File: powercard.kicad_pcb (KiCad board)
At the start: 4 copper layers, 90 x 54.3 mm, 105 parts, among them J1 EDGE, J2 PDI, J3 DBG, Q1 CSD18503Q5A, Q2 CSD18503Q5A, Q3 CSD18503Q5A, Q4 CSD18503Q5A, Q5 BSS84, Q6 2N7002, Q7 2N7002, U1 RT7258GQW, U2 RT7258GQW, U3 RT7258GQW, U4 RT7258GQW, U5 74HCT1G02, U6 RT7258GQW, U7 ATXMEGA32E5-MU, U8 MCP1754ST-3302E/CB

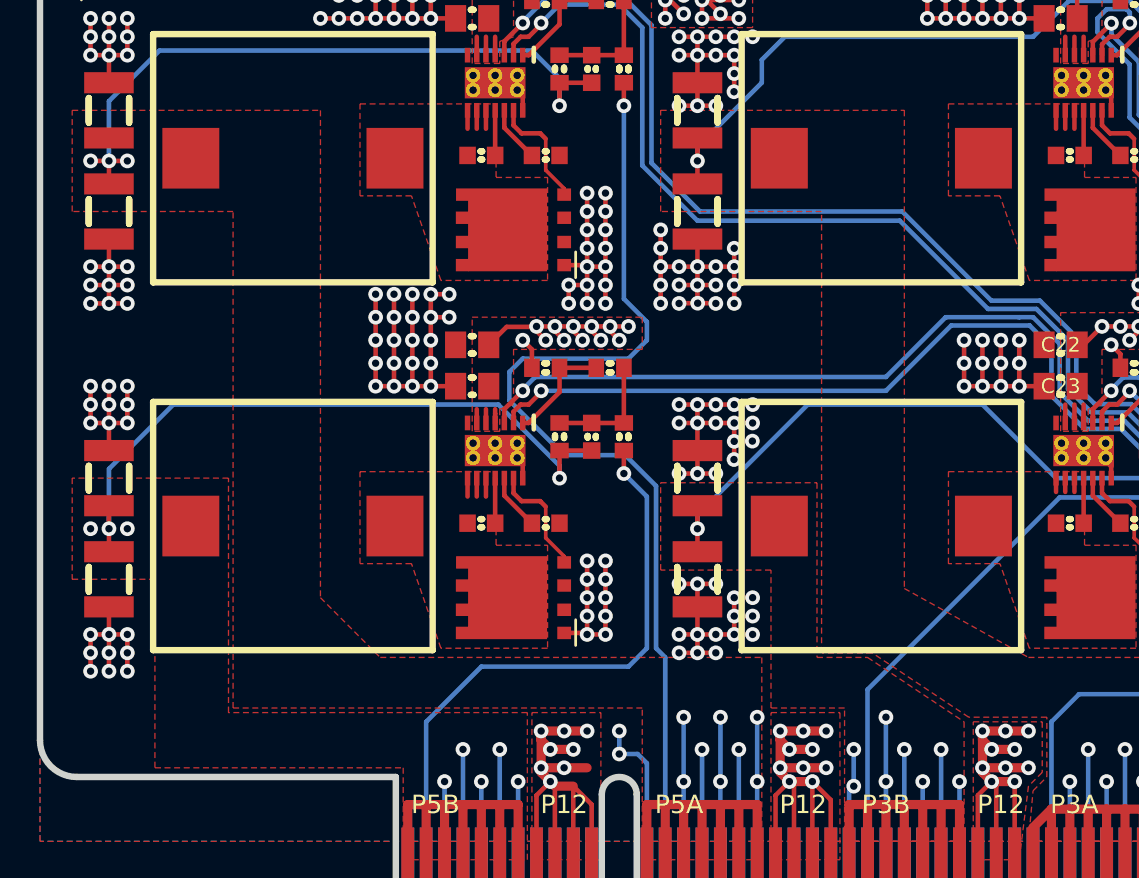
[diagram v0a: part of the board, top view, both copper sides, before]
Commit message: Layout tweaks
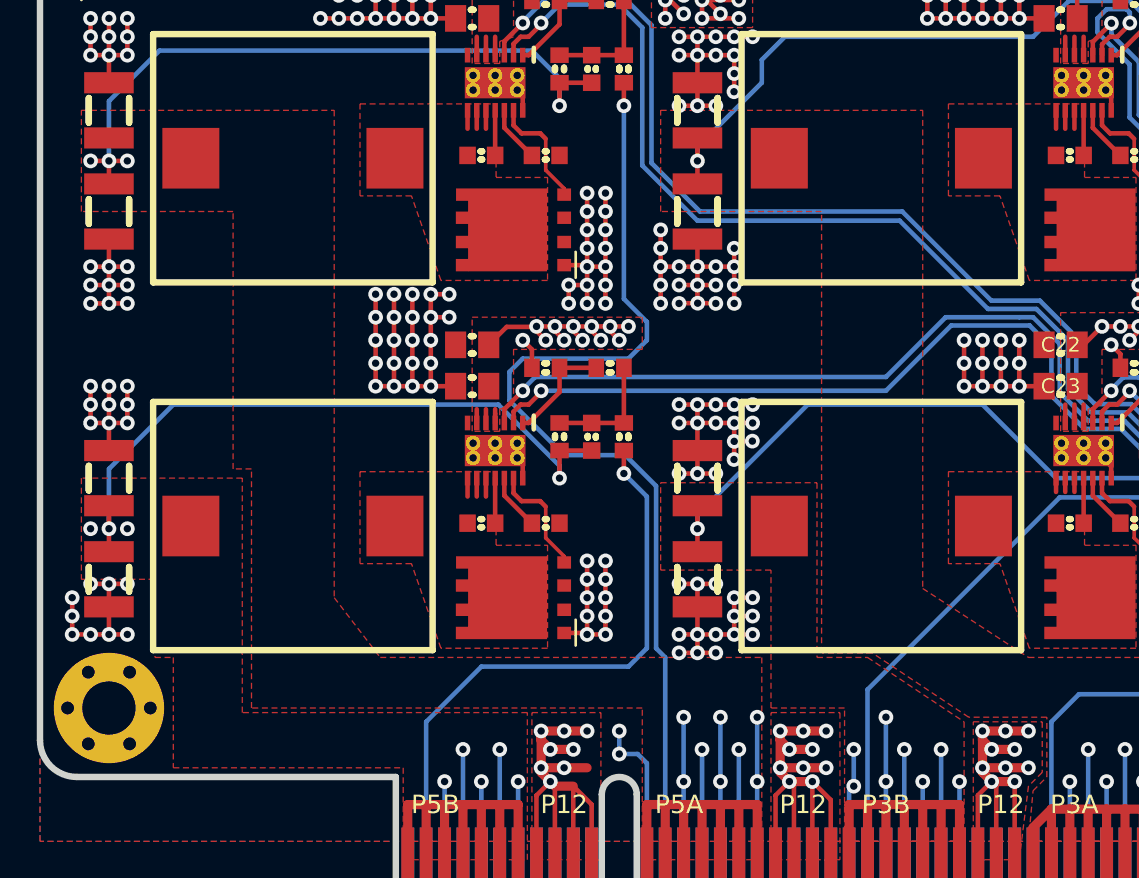
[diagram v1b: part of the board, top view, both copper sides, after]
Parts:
- added MP1: SCREW, mech:SCREW-3-SUPPORTED, F.Cu at (51.8, 89.2)

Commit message: More PCB tweaks
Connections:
- J1 pad A45: Net-(J1-PadA45) -> GND
- J1 pad A46: /INT# -> GND
- J1 pad A47: /SCL -> /INT#
- J1 pad A48: /SDA -> /SCL
- J1 pad A49: GND -> /SDA
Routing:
- net GND: track 493.8 -> 496.5 mm, vias 305 -> 317
- net /INT#: track 16.3 -> 14.6 mm
- net /SCL: track 16.2 -> 15.1 mm
- net /SDA: track 15.7 -> 15.1 mm
- net /N12V_1A: vias 13 -> 12
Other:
- board text added: "+12"
- board text added: "+3A"
- board text added: "+3B"
- board text added: "+5A"
- board text added: "+5B"
- board text added: "12"
- board text removed: "G"
- board text removed: "INT"
- board text removed: "N12"
- board text removed: "N12s"
- board text removed: "P12"
- board text removed: "P3A"
- board text removed: "P3As"
- board text removed: "P3B"
- board text removed: "P3Bs"
- board text removed: "P5A"
- board text removed: "P5As"
- board text removed: "P5B"
- board text removed: "P5Bs"
- board text removed: "SCL"
- board text removed: "SDA"

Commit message: Even more PCB tweaks
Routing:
- net GND: track 496.5 -> 497.5 mm
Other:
- board text added: "A 3V3 B"
- board text added: "A 5V B"
- board text added: "C4-0 POWER SUPPLY REV 1.0 JULY 2016"
- board text added: "N12"
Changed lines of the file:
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@@
     (area 47.824999 46.824999 138.175001 101.525001)
     (thickness 1.6)
-    (drawings 112)
-    (tracks 1902)
+    (drawings 150)
+    (tracks 1910)
     (zones 0)
     (modules 106)
@@
     (35 F.Paste user)
     (36 B.SilkS user)
-    (37 F.SilkS user)
+    (37 F.SilkS user hide)
     (38 B.Mask user)
     (39 F.Mask user)
@@
     (45 Margin user)
     (46 B.CrtYd user)
-    (47 F.CrtYd user hide)
+    (47 F.CrtYd user)
     (48 B.Fab user)
     (49 F.Fab user hide)
@@
     )
   )
+  (gr_line (start 107 90.75) (end 107.75 91) (layer F.Mask) (width 0.5))
+  (gr_line (start 107 92.25) (end 107.75 92) (layer F.Mask) (width 0.5))
+  (gr_line (start 107.75 90.5) (end 107.75 92.25) (layer F.Mask) (width 0.5))
+  (gr_line (start 108 92.25) (end 107 92.5) (layer F.Mask) (width 0.5))
+  (gr_line (start 108 90.5) (end 108 92.25) (layer F.Mask) (width 0.5))
+  (gr_line (start 107 90.5) (end 107.75 90.5) (layer F.Mask) (width 1))
+  (gr_line (start 106 90.75) (end 107 90.5) (layer F.Mask) (width 1))
+  (gr_line (start 105 90.5) (end 106 90.75) (layer F.Mask) (width 1))
+  (gr_line (start 104 90.75) (end 105 90.5) (layer F.Mask) (width 1))
+  (gr_line (start 94 88.75) (end 95 89) (layer F.Mask) (width 1))
+  (gr_line (start 93 89) (end 94 88.75) (layer F.Mask) (width 1))
+  (gr_line (start 50.75 51.5) (end 50.75 52) (layer F.Mask) (width 0.2))
+  (gr_line (start 51 52) (end 50.75 51.5) (layer F.Mask) (width 0.2))
+  (gr_line (start 50.5 52) (end 51 52) (layer F.Mask) (width 0.2))
+  (gr_line (start 50.75 51.5) (end 50.5 52) (layer F.Mask) (width 0.2))
+  (gr_line (start 127.25 59.75) (end 127.25 60.25) (layer F.Mask) (width 0.2))
+  (gr_line (start 127.25 60.25) (end 127 60) (layer F.Mask) (width 0.2))
+  (gr_line (start 127 60) (end 127.25 59.75) (layer F.Mask) (width 0.2))
+  (gr_line (start 128.5 84) (end 129.25 84) (layer F.Mask) (width 0.2))
+  (gr_line (start 129.25 84.25) (end 128.5 84) (layer F.Mask) (width 0.2))
+  (gr_line (start 129.25 83.75) (end 129.25 84.25) (layer F.Mask) (width 0.2))
+  (gr_line (start 128.5 84) (end 129.25 83.75) (layer F.Mask) (width 0.2))
+  (gr_line (start 75.25 54.25) (end 75.25 54.75) (layer F.Mask) (width 0.2))
+  (gr_line (start 75 54.5) (end 75.25 54.25) (layer F.Mask) (width 0.2))
+  (gr_line (start 75.25 54.75) (end 75 54.5) (layer F.Mask) (width 0.2))
+  (gr_line (start 75.25 74.25) (end 75.25 74.75) (layer F.Mask) (width 0.2))
+  (gr_line (start 75 74.5) (end 75.25 74.25) (layer F.Mask) (width 0.2))
+  (gr_line (start 75.25 74.75) (end 75 74.5) (layer F.Mask) (width 0.2))
+  (gr_line (start 107.25 74.25) (end 107.25 74.75) (layer F.Mask) (width 0.2))
+  (gr_line (start 107 74.5) (end 107.25 74.25) (layer F.Mask) (width 0.2))
+  (gr_line (start 107.25 74.75) (end 107 74.5) (layer F.Mask) (width 0.2))
+  (gr_line (start 107 54.25) (end 107.25 54) (layer F.Mask) (width 0.2))
+  (gr_line (start 107.25 54.5) (end 107 54.25) (layer F.Mask) (width 0.2))
+  (gr_line (start 107.25 54) (end 107.25 54.5) (layer F.Mask) (width 0.2))
+  (gr_text N12 (at 124.5 49.75 90) (layer F.Mask)
+    (effects (font (size 1.1 1.1) (thickness 0.275)))
+  )
+  (gr_text "A\n3V3\nB" (at 88.5 69.5) (layer F.Mask)
+    (effects (font (size 1.1 1.1) (thickness 0.275)))
+  )
+  (gr_text "A\n5V\nB" (at 56 69.5) (layer F.Mask)
+    (effects (font (size 1.1 1.1) (thickness 0.275)))
+  )
+  (gr_text "C4-0 POWER SUPPLY\nREV 1.0 JULY 2016" (at 65.25 59.5) (layer B.Mask)
+    (effects (font (size 1.5 1.5) (thickness 0.3)) (justify mirror))
+  )
   (gr_line (start 113.25 93.5) (end 114.25 93.5) (layer F.Mask) (width 0.2))
   (gr_line (start 103.25 92.5) (end 103 94.75) (layer F.Mask) (width 0.75))
@@
   (segment (start 67.99826 97.75) (end 67.99826 94.50174) (width 0.5) (layer F.Cu) (net 1))
   (segment (start 76.25 75.25) (end 78 75.25) (width 0.25) (layer F.Cu) (net 1))
+  (segment (start 52.75 51.75) (end 53.75 51.75) (width 0.25) (layer F.Cu) (net 2))
+  (via (at 53.75 51.75) (size 0.8) (drill 0.4) (layers F.Cu B.Cu) (net 2))
   (segment (start 110.75 80.5) (end 110.75 79.5) (width 0.25) (layer F.Cu) (net 2))
   (via (at 110.75 79.5) (size 0.8) (drill 0.4) (layers F.Cu B.Cu) (net 2))
@@
   (via (at 52.75 51.75) (size 0.8) (drill 0.4) (layers F.Cu B.Cu) (net 2))
   (segment (start 50.75 52.75) (end 50.75 51.75) (width 0.25) (layer F.Cu) (net 2))
-  (via (at 50.75 51.75) (size 0.8) (drill 0.4) (layers F.Cu B.Cu) (net 2))
   (segment (start 51.75 52.75) (end 51.75 51.75) (width 0.25) (layer F.Cu) (net 2))
   (via (at 51.75 51.75) (size 0.8) (drill 0.4) (layers F.Cu B.Cu) (net 2))
@@
   (segment (start 79.75 53.75) (end 78 53.75) (width 0.25) (layer F.Cu) (net 28))
   (segment (start 76.25 53.75) (end 78 53.75) (width 0.25) (layer F.Cu) (net 28))
-  (segment (start 106.25 53.75) (end 106.573002 53.75) (width 0.25) (layer F.Cu) (net 29))
-  (segment (start 106.573002 53.75) (end 108.25 52.073002) (width 0.25) (layer F.Cu) (net 29))
+  (segment (start 106.25 53.75) (end 106.25 53.5) (width 0.25) (layer F.Cu) (net 29))
+  (segment (start 107.598162 52.72484) (end 108.25 52.073002) (width 0.25) (layer F.Cu) (net 29))
+  (segment (start 106.25 53.5) (end 106.54999 53.20001) (width 0.25) (layer F.Cu) (net 29))
+  (segment (start 106.54999 53.20001) (end 106.759402 53.20001) (width 0.25) (layer F.Cu) (net 29))
+  (segment (start 106.759402 53.20001) (end 107.234572 52.72484) (width 0.25) (layer F.Cu) (net 29))
+  (segment (start 107.234572 52.72484) (end 107.598162 52.72484) (width 0.25) (layer F.Cu) (net 29))
   (segment (start 108.25 52.073002) (end 108.25 50.75) (width 0.25) (layer F.Cu) (net 29))
   (segment (start 108.25 50.75) (end 110.25 50.75) (width 0.25) (layer F.Cu) (net 29))
@@
   (segment (start 127.95 87.25) (end 128.997213 87.25) (width 0.25) (layer F.Cu) (net 65))
   (via (at 129.767559 86.479654) (size 0.8) (drill 0.4) (layers F.Cu B.Cu) (net 65))
+  (segment (start 105.25 53.02532) (end 105.52532 52.75) (width 0.25) (layer F.Cu) (net 66))
+  (segment (start 105.73734 52.01266) (end 105.52532 52.22468) (width 0.25) (layer F.Cu) (net 66))
+  (segment (start 105.52532 52.22468) (end 105.52532 52.75) (width 0.25) (layer F.Cu) (net 66))
+  (segment (start 106.26266 52.01266) (end 105.73734 52.01266) (width 0.25) (layer F.Cu) (net 66))
   (segment (start 114.75 70.5) (end 114.250001 70.000001) (width 0.25) (layer B.Cu) (net 66))
   (segment (start 108.5 57.75) (end 107.75 57) (width 0.25) (layer B.Cu) (net 66))
@@
   (segment (start 124 80.25) (end 123.63641 80.25) (width 0.25) (layer B.Cu) (net 66))
   (segment (start 123.63641 80.25) (end 122.800052 79.413642) (width 0.25) (layer B.Cu) (net 66))
-  (segment (start 105.25 53.02532) (end 106.26266 52.01266) (width 0.25) (layer F.Cu) (net 66))
   (segment (start 105.25 53.75) (end 105.25 53.02532) (width 0.25) (layer F.Cu) (net 66))
   (via (at 106.26266 52.01266) (size 0.8) (drill 0.4) (layers F.Cu B.Cu) (net 66))
@@
       (pts
         (xy 126.6 65.4) (xy 126.6 69.8) (xy 132.8 69.8) (xy 132.8 59.6) (xy 130.8 59.6)
-        (xy 130.8 60.4) (xy 127.6 60.4) (xy 127 59.8) (xy 123.4 59.8) (xy 123.4 61.2)
-        (xy 126.6 61.2) (xy 126.6 63.4)
+        (xy 130.8 60.4) (xy 127.6 60.4) (xy 127.6 59.8) (xy 127.4 59.4) (xy 123.4 59.4)
+        (xy 123.4 61.2) (xy 126.6 61.2) (xy 126.6 63.4)
       )
     )
@@
     (polygon
       (pts
-        (xy 127.4 59.6) (xy 130.6 59.6) (xy 130.8 59.4) (xy 132.8 59.4) (xy 132.8 56)
+        (xy 127.8 59.6) (xy 130.6 59.6) (xy 130.8 59.4) (xy 132.8 59.4) (xy 132.8 56)
         (xy 135.75 56) (xy 135.75 53.25) (xy 131.75 53.25) (xy 131.75 54.75) (xy 128.6 58)
-        (xy 127.4 58)
+        (xy 127.8 58)
       )
     )

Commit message: Commit R1.0 sent to fab
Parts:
- added DS3: 3VA, smd-semi:LED-0603, F.Cu at (92.0, 15.0)
- added DS4: 3VB, smd-semi:LED-0603, F.Cu at (92.0, 17.0)
- added DS5: N12, smd-semi:LED-0603, F.Cu at (92.0, 19.0)
- added DS6: SFY, smd-semi:LED-0603, F.Cu at (92.0, 21.0)
- added R35: 1k, IPC7351-Nominal:RESC1608X50, F.Cu at (92.5, 25.0)
- C14, C21, C28, C7: value C-0603 -> 1u
- DS1: value R -> 5VA
- DS2: value G -> 5VB
- R1, R13, R5, R9: value R-0603 -> 1k
- R10, R14: value R-0603 -> 62k
- R11, R15: value R-0603 -> 20k
- R12, R16, R4, R8: value R-0603 -> 100
- R2, R6: value R-0603 -> 95k3
- R3, R7: value R-0603 -> 18k
- R33, R34: value 2k2 -> 1k
- moved J1 83.2 mm to (14.5, 45.2)
- moved R32 70.0 mm to (97.8, 31.0), turned to 270 degrees
- moved C42 69.7 mm to (82.5, 41.5), turned to 270 degrees
- moved C16 68.1 mm to (54.2, 4.75)
- moved C2 68.1 mm to (22.2, 22.5)
- moved C22 68.1 mm to (54.2, 22.5)
- moved C23 68.1 mm to (54.2, 24.8)
- moved C3 68.1 mm to (22.2, 24.8)
- moved C8 68.1 mm to (22.2, 2.50)
- moved C9 68.1 mm to (22.2, 4.75)
- moved C15 67.9 mm to (54.2, 2.75)
- moved R2 67.5 mm to (31.0, 23.2)
- moved R3 67.5 mm to (27.5, 23.2)
- moved R6 67.4 mm to (31.0, 3.50)
- moved R7 67.4 mm to (27.5, 3.50)
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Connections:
- net /Controller/DBGRX renamed /Supervisor/DBGRX
- net /Controller/DBGTX renamed /Supervisor/DBGTX
- net /Controller/PDIC renamed /Supervisor/PDIC
- net /Controller/PDID renamed /Supervisor/PDID
- DS1 pad 1: GND -> Net-(DS1-Pad1)
- DS2 pad 1: GND -> Net-(DS2-Pad1)
- DS2 pad 2: Net-(DS2-Pad2) -> Net-(DS1-Pad1)
- J1 pad A14: GND -> /5VSENSE_2
- J1 pad A2: /5VSENSE_2 -> GND
- J1 pad A24: /3V3SENSE_2 -> GND
- J1 pad A34: /3V3SENSE_1 -> GND
- J1 pad A36: GND -> /3V3SENSE_1
- J1 pad A37: GND -> /3V3SENSE_2
- R33 pad 1: /Controller/LED_R -> Net-(DS1-Pad2)
- R33 pad 2: Net-(DS1-Pad2) -> /Supervisor/LED_A
- R34 pad 1: /Controller/LED_G -> Net-(DS1-Pad1)
- R34 pad 2: Net-(DS2-Pad2) -> /Supervisor/LED_B
- U1 pad 3: /Controller/CLK1 -> /Supervisor/CLK1
- U2 pad 3: /Controller/CLK2 -> /Supervisor/CLK2
- U3 pad 3: /N12V_1A/CLK -> /Supervisor/CLK4
- U4 pad 3: /Controller/CLK3 -> /N12V_1A/CLK
- U7 pad 10: /Controller/CLK3 -> /Supervisor/CLK4
- U7 pad 11: /Controller/CLK2 -> /Supervisor/CLK1
- U7 pad 12: /Controller/CLK1 -> /Supervisor/CLK2
- U7 pad 2: /Controller/LED_R -> /Supervisor/LED_B
- U7 pad 24: /5V_8A_2/PG -> /5V_8A_1/PG
- U7 pad 25: /5V_8A_1/PG -> /5V_8A_2/PG
- U7 pad 26: /3V3_8A_2/PG -> /3V3_8A_1/PG
- U7 pad 27: /3V3_8A_1/PG -> /3V3_8A_2/PG
- U7 pad 3: /Controller/LED_G -> /Supervisor/LED_C
- U7 pad 4: Net-(U7-Pad4) -> /Supervisor/LED_A
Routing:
- net /Supervisor/CLK4: track 0.00 -> 187.5 mm, vias 0 -> 2
- net /Supervisor/CLK1: track 0.00 -> 131.2 mm, vias 0 -> 2
- net /Supervisor/CLK2: track 0.00 -> 115.8 mm, vias 0 -> 2
- net /Controller/LED_G: track 114.3 -> 0.00 mm, vias 2 -> 0
- net /Controller/LED_R: track 111.7 -> 0.00 mm, vias 2 -> 0
- net /Controller/CLK2: track 77.0 -> 0.00 mm, vias 2 -> 0
- net /Controller/CLK1: track 66.6 -> 0.00 mm, vias 2 -> 0
- net /N12V_1A/CLK: track 47.6 -> 96.9 mm
- net /N12V_1A: track 78.6 -> 125.6 mm, vias 12 -> 20
- net /SDA: track 15.1 -> 58.2 mm, vias 1 -> 2
- net /SCL: track 15.1 -> 54.9 mm, vias 1 -> 2
- net /3V3_8A_2/PG: track 39.3 -> 77.8 mm
- net /INT#: track 14.6 -> 51.9 mm
- net /5V_8A_2/PG: track 81.9 -> 118.0 mm
- net /Controller/CLK3: track 30.6 -> 0.00 mm, vias 2 -> 0
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- added copper zone on In2.Cu, net /12V
- added copper zone on In2.Cu, net /N12V_1A
- added copper zone on In1.Cu, net GND
- removed copper zone on VIN.Cu, net /12V
- removed copper zone on VIN.Cu, net /N12V_1A
- removed copper zone on GND.Cu, net GND
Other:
- board size 90 x 54.3 mm -> 100 x 49.4 mm
- net class Default: clearance 0.2 -> 0.199
- rule pad_to_mask_clearance: 0.2 -> 0.03175
- rule trace_clearance: 0.2 -> 0.199
- board text added: "1"
- board text added: "2"
- board text added: "3"
- board text added: "3V3/9600/8N1"
- board text added: "3VA"
- board text added: "3VB"
- board text added: "4"
- board text added: "5VA"
- board text added: "5VB"
- board text added: "C4-0 PSU R1.0 JUL 2016"
- board text added: "DBG"
- board text added: "IN OUT GND"
- board text added: "SFY"
- board text removed: "+12"
- board text removed: "+3A"
- board text removed: "+3B"
- board text removed: "+5A"
- board text removed: "+5B"
- board text removed: "12"
- board text removed: "C4-0 POWER SUPPLY REV 1.0 JULY 2016"

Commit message: Final rev take 2
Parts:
- added R36: 5k1, IPC7351-Nominal:RESC1608X50, F.Cu at (73.0, 12.2)
- C38: value C-0603 -> DNP
- R25, R28: value R-0603 -> 0R
- R26: value R-0603 -> 3k6
- R27: value R-0603 -> 51k
- moved C38 2.00 mm to (73.0, 14.5)
- moved R25 1.75 mm to (73.0, 16.2)
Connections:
- U6 pad 2: Net-(Q7-Pad2) -> Net-(R36-Pad2)
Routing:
- net Net-(R36-Pad2): track 0.00 -> 12.3 mm, vias 0 -> 2
- net Net-(Q7-Pad2): track 11.6 -> 5.44 mm, vias 2 -> 0
- net /Supervisor/CLK4: track 187.5 -> 183.5 mm
- net Net-(C38-Pad2): track 6.50 -> 7.27 mm
- net Net-(Q6-Pad3): track 24.9 -> 24.2 mm
- net /N12V_1A/V-: track 10.4 -> 11.0 mm
- net /N12V_1A/VIN: track 20.7 -> 20.2 mm
